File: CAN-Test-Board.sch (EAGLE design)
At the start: 52 parts, among them Y1 ECS-80-S-4X, Y2 ECS-80-S-4X

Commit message: couple part values
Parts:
- C12: value 100nF -> 0.1uF
- R14: value (none) -> 0
- R7, R9: value (none) -> 330
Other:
- moved on the sheet: R14
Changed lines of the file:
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@@
 <part name="R3" library="SparkFun-Resistors" library_urn="urn:adsk.eagle:library:532" deviceset="1KOHM" device="-0603-1/10W-1%" package3d_urn="urn:adsk.eagle:package:39650/1" value="1k"/>
 <part name="D1" library="SparkFun-LED" library_urn="urn:adsk.eagle:library:529" deviceset="LED" device="0603" package3d_urn="urn:adsk.eagle:package:39354/1"/>
-<part name="R7" library="SparkFun-Resistors" library_urn="urn:adsk.eagle:library:532" deviceset="RESISTOR" device="0603" package3d_urn="urn:adsk.eagle:package:39650/1" value=" "/>
+<part name="R7" library="SparkFun-Resistors" library_urn="urn:adsk.eagle:library:532" deviceset="RESISTOR" device="0603" package3d_urn="urn:adsk.eagle:package:39650/1" value="330"/>
 <part name="GND11" library="supply2" library_urn="urn:adsk.eagle:library:372" deviceset="GND" device=""/>
 <part name="FRAME2" library="SparkFun-Aesthetics" library_urn="urn:adsk.eagle:library:507" deviceset="FRAME-A4L" device=""/>
 <part name="U$1" library="PI_Shield_Library" deviceset="MCP2515" device=""/>
-<part name="C12" library="SparkFun-Capacitors" library_urn="urn:adsk.eagle:library:510" deviceset="22NF/22,000PF" device="-0603-50V-10%" package3d_urn="urn:adsk.eagle:package:37414@1/1" value="100nF"/>
+<part name="C12" library="SparkFun-Capacitors" library_urn="urn:adsk.eagle:library:510" deviceset="22NF/22,000PF" device="-0603-50V-10%" package3d_urn="urn:adsk.eagle:package:37414@1/1" value="0.1uF"/>
 <part name="GND5" library="supply1" library_urn="urn:adsk.eagle:library:371" deviceset="GND" device=""/>
 <part name="GND10" library="supply1" library_urn="urn:adsk.eagle:library:371" deviceset="GND" device=""/>
@@
 <part name="GND22" library="SparkFun-PowerSymbols" library_urn="urn:adsk.eagle:library:530" deviceset="GND" device=""/>
 <part name="D2" library="SparkFun-LED" library_urn="urn:adsk.eagle:library:529" deviceset="LED" device="0603" package3d_urn="urn:adsk.eagle:package:39354/1"/>
-<part name="R9" library="SparkFun-Resistors" library_urn="urn:adsk.eagle:library:532" deviceset="RESISTOR" device="0603" package3d_urn="urn:adsk.eagle:package:39650/1" value=" "/>
+<part name="R9" library="SparkFun-Resistors" library_urn="urn:adsk.eagle:library:532" deviceset="RESISTOR" device="0603" package3d_urn="urn:adsk.eagle:package:39650/1" value="330"/>
 <part name="GND23" library="supply2" library_urn="urn:adsk.eagle:library:372" deviceset="GND" device=""/>
 <part name="J1" library="SparkFun-Connectors" library_urn="urn:adsk.eagle:library:513" deviceset="CONN_12" device="" package3d_urn="urn:adsk.eagle:package:38169/1"/>
@@
 <part name="J4" library="SparkFun-Connectors" library_urn="urn:adsk.eagle:library:513" deviceset="CONN_03" device="" package3d_urn="urn:adsk.eagle:package:38063/1"/>
 <part name="J5" library="SparkFun-Connectors" library_urn="urn:adsk.eagle:library:513" deviceset="CONN_03" device="" package3d_urn="urn:adsk.eagle:package:38063/1"/>
-<part name="R14" library="SparkFun-Resistors" library_urn="urn:adsk.eagle:library:532" deviceset="RESISTOR" device="0603" package3d_urn="urn:adsk.eagle:package:39650/1" value=" "/>
+<part name="R14" library="SparkFun-Resistors" library_urn="urn:adsk.eagle:library:532" deviceset="RESISTOR" device="0603" package3d_urn="urn:adsk.eagle:package:39650/1" value="0"/>
 <part name="R15" library="SparkFun-Resistors" library_urn="urn:adsk.eagle:library:532" deviceset="RESISTOR" device="0603" package3d_urn="urn:adsk.eagle:package:39650/1" value="0"/>
 <part name="U$4" library="Samtec t2i" deviceset="T2I" device="" package3d_urn="urn:adsk.eagle:package:23194708/2"/>
@@
 <attribute name="NAME" x="20.32" y="137.668" size="1.778" layer="95" font="vector"/>
 </instance>
-<instance part="R14" gate="G$1" x="241.3" y="55.88" smashed="yes" rot="R180">
-<attribute name="NAME" x="241.3" y="54.356" size="1.778" layer="95" font="vector" rot="R180" align="bottom-center"/>
-<attribute name="VALUE" x="241.3" y="57.404" size="1.778" layer="96" font="vector" rot="R180" align="top-center"/>
+<instance part="R14" gate="G$1" x="241.3" y="55.88" smashed="yes" rot="MR0">
+<attribute name="NAME" x="241.3" y="57.404" size="1.778" layer="95" font="vector" rot="MR0" align="bottom-center"/>
+<attribute name="VALUE" x="241.3" y="54.356" size="1.778" layer="96" font="vector" rot="MR0" align="top-center"/>
 </instance>
 <instance part="U$4" gate="G$1" x="25.4" y="154.94" smashed="yes">

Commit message: couple changes for a possible rev 2 (led sizes, button footprint)
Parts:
- C13, C14: device Resistor_Capacitor:C0603C180J5GACTU -> SparkFun-Capacitors:22NF/22,000PF-0603-50V-10%
- C15: value 100nF -> 0.1uF
- D1, D2: value (none) -> LED-0805; device SparkFun-LED:LED0603 -> LED-0805:LED-0805
- RESET: value SWITCH -> DISCRETECOMPONENTS_SWITCH; device DiscreteComponents:SWITCH -> Push button:DISCRETECOMPONENTS_SWITCH

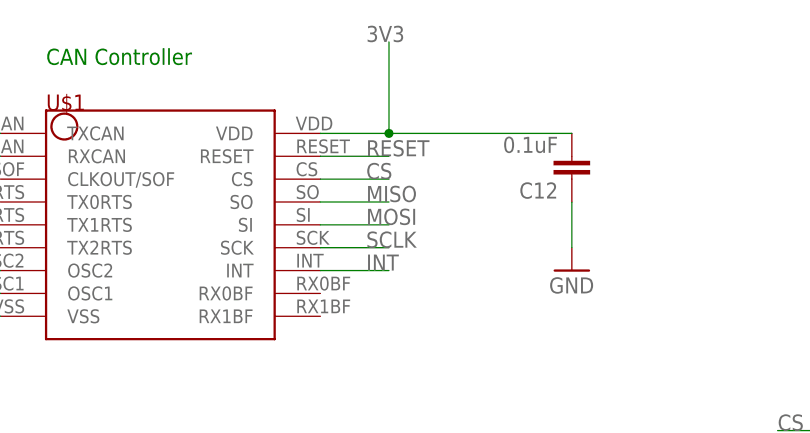
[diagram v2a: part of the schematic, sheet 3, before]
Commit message: Shorted Reset to 3V3 instead of leaving it floating
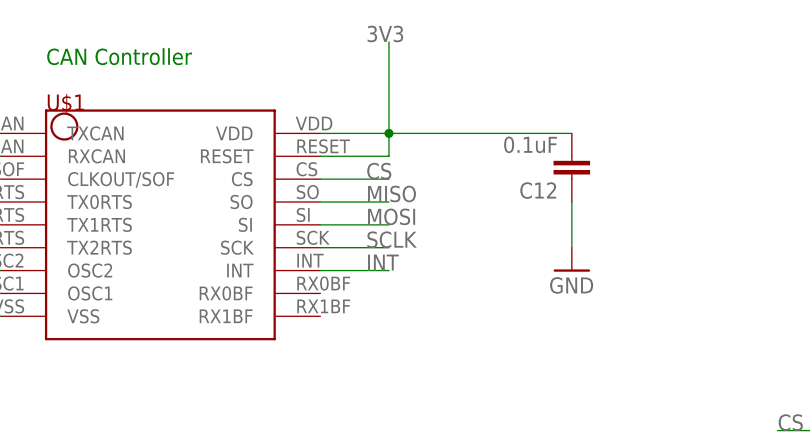
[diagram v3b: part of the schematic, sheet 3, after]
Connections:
- removed net RESET: U$1.RESET
- net 3V3: now also U$1.RESET
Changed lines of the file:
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@@
-</segment>
-</net>
-<net name="RESET" class="0">
-<segment>
-<pinref part="U$1" gate="G$1" pin="RESET"/>
-<wire x1="193.04" y1="162.56" x2="200.66" y2="162.56" width="0.1524" layer="91"/>
-<label x="198.12" y="162.56" size="1.778" layer="95"/>
 </segment>
 </net>
@@
 <junction x="200.66" y="165.1"/>
 <label x="198.12" y="175.26" size="1.778" layer="95"/>
+<pinref part="U$1" gate="G$1" pin="RESET"/>
+<wire x1="193.04" y1="162.56" x2="200.66" y2="162.56" width="0.1524" layer="91"/>
+<wire x1="200.66" y1="162.56" x2="200.66" y2="165.1" width="0.1524" layer="91"/>
 </segment>
 <segment>

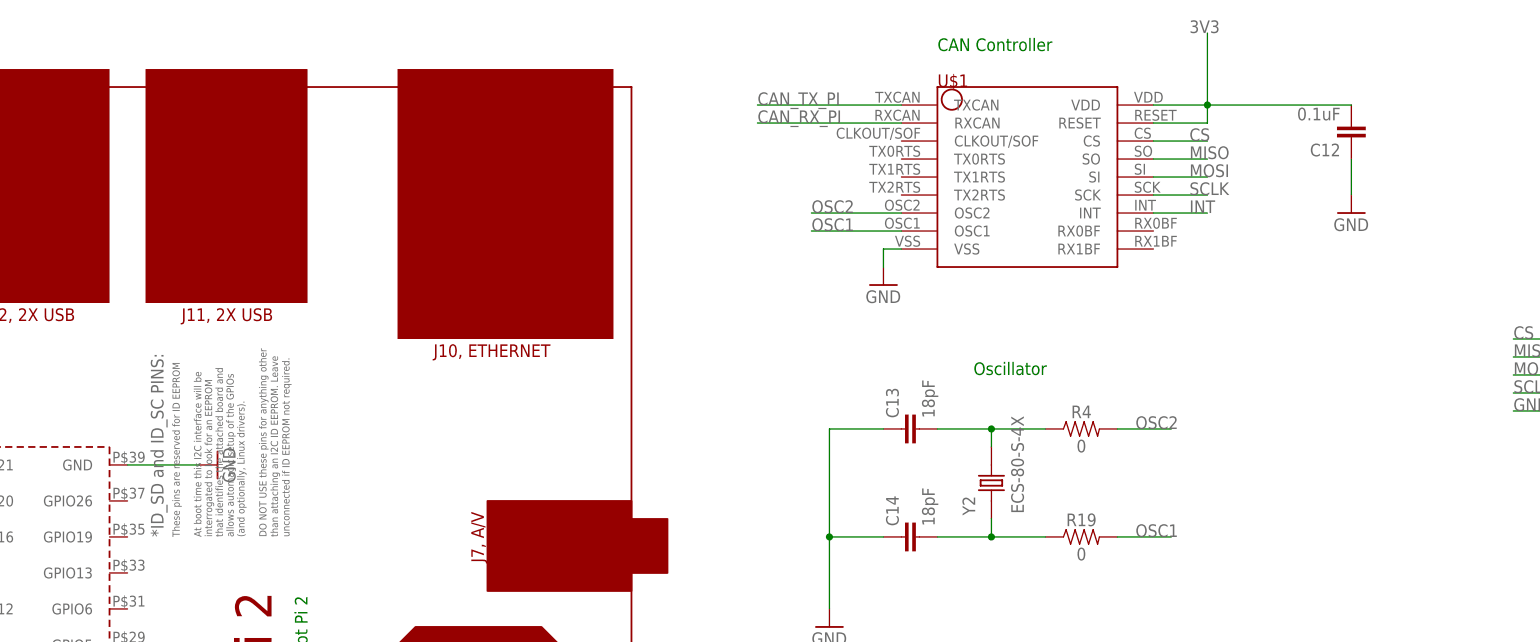
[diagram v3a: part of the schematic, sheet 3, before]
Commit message: Add missing interrupt connection
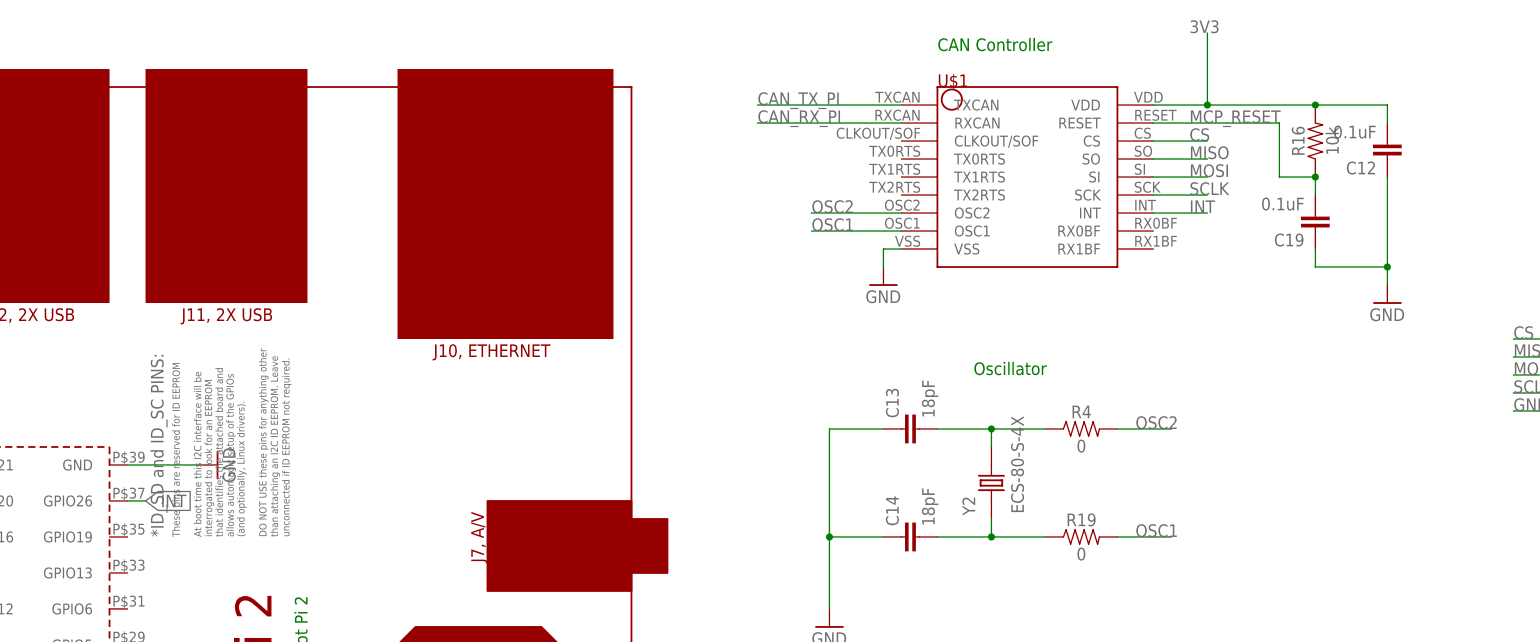
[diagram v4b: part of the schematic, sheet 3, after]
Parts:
- added C19: 0.1uF, SparkFun-Capacitors:22NF/22,000PF-0603-50V-10%
- added R16: 10k, SparkFun-Resistors:1KOHM-0603-1/10W-1%
- C7: value 4.7uF -> 0.1uF
- R2: value 1k -> 10k
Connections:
- new net MCP_RESET: C19.2, R16.1, U$1.RESET
- net 3V3: now also R16.2; no longer U$1.RESET
- net GND: now also C19.1
- net INT: now also PCB1.GPIO26
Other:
- moved on the sheet: C12
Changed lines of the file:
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@@
 <?xml version="1.0" encoding="utf-8"?>
 <!DOCTYPE eagle SYSTEM "eagle.dtd">
-<eagle version="9.6.2">
+<eagle version="9.6.0">
 <drawing>
 <settings>
@@
 <part name="GND1" library="supply2" library_urn="urn:adsk.eagle:library:372" deviceset="GND" device=""/>
 <part name="GND2" library="supply2" library_urn="urn:adsk.eagle:library:372" deviceset="GND" device=""/>
-<part name="C7" library="SparkFun-Capacitors" library_urn="urn:adsk.eagle:library:510" deviceset="4.7UF" device="0603" package3d_urn="urn:adsk.eagle:package:37414@2/1" value="4.7uF"/>
+<part name="C7" library="SparkFun-Capacitors" library_urn="urn:adsk.eagle:library:510" deviceset="4.7UF" device="0603" package3d_urn="urn:adsk.eagle:package:37414@2/1" value="0.1uF"/>
 <part name="GND3" library="supply2" library_urn="urn:adsk.eagle:library:372" deviceset="GND" device=""/>
 <part name="SV1" library="con-lsta" library_urn="urn:adsk.eagle:library:161" deviceset="FE05-1" device="" package3d_urn="urn:adsk.eagle:package:8190/1"/>
@@
 <part name="R1" library="SparkFun-Resistors" library_urn="urn:adsk.eagle:library:532" deviceset="1KOHM" device="-0603-1/10W-1%" package3d_urn="urn:adsk.eagle:package:39650/1" value="1k"/>
 <part name="+3V1" library="supply1" library_urn="urn:adsk.eagle:library:371" deviceset="+3V3" device=""/>
-<part name="R2" library="SparkFun-Resistors" library_urn="urn:adsk.eagle:library:532" deviceset="1KOHM" device="-0603-1/10W-1%" package3d_urn="urn:adsk.eagle:package:39650/1" value="1k"/>
+<part name="R2" library="SparkFun-Resistors" library_urn="urn:adsk.eagle:library:532" deviceset="1KOHM" device="-0603-1/10W-1%" package3d_urn="urn:adsk.eagle:package:39650/1" value="10k"/>
 <part name="+3V2" library="supply1" library_urn="urn:adsk.eagle:library:371" deviceset="+3V3" device=""/>
 <part name="R3" library="SparkFun-Resistors" library_urn="urn:adsk.eagle:library:532" deviceset="1KOHM" device="-0603-1/10W-1%" package3d_urn="urn:adsk.eagle:package:39650/1" value="1k"/>
@@
 <part name="D2" library="LED-0805" deviceset="LED-0805" device=""/>
 <part name="RESET" library="Push button" deviceset="DISCRETECOMPONENTS_SWITCH" device=""/>
+<part name="C19" library="SparkFun-Capacitors" library_urn="urn:adsk.eagle:library:510" deviceset="22NF/22,000PF" device="-0603-50V-10%" package3d_urn="urn:adsk.eagle:package:37414@1/1" value="0.1uF"/>
+<part name="R16" library="SparkFun-Resistors" library_urn="urn:adsk.eagle:library:532" deviceset="1KOHM" device="-0603-1/10W-1%" package3d_urn="urn:adsk.eagle:package:39650/1" value="10k"/>
 </parts>
 <sheets>
@@
 <attribute name="NAME" x="162.56" y="167.64" size="1.778" layer="94"/>
 </instance>
-<instance part="C12" gate="G$1" x="220.98" y="162.56" smashed="yes" rot="R180">
-<attribute name="NAME" x="219.456" y="159.639" size="1.778" layer="95" font="vector" rot="R180"/>
-<attribute name="VALUE" x="219.456" y="164.719" size="1.778" layer="96" font="vector" rot="R180"/>
-</instance>
-<instance part="GND5" gate="1" x="220.98" y="149.86" smashed="yes">
-<attribute name="VALUE" x="218.44" y="147.32" size="1.778" layer="96"/>
+<instance part="C12" gate="G$1" x="226.06" y="160.02" smashed="yes" rot="R180">
+<attribute name="NAME" x="224.536" y="157.099" size="1.778" layer="95" font="vector" rot="R180"/>
+<attribute name="VALUE" x="224.536" y="162.179" size="1.778" layer="96" font="vector" rot="R180"/>
+</instance>
+<instance part="GND5" gate="1" x="226.06" y="137.16" smashed="yes">
+<attribute name="VALUE" x="223.52" y="134.62" size="1.778" layer="96"/>
 </instance>
 <instance part="GND10" gate="1" x="154.94" y="139.7" smashed="yes">
@@
 <attribute name="NAME" x="157.099" y="105.664" size="1.778" layer="95" font="vector" rot="R90"/>
 <attribute name="VALUE" x="162.179" y="105.664" size="1.778" layer="96" font="vector" rot="R90"/>
+</instance>
+<instance part="C19" gate="G$1" x="215.9" y="149.86" smashed="yes" rot="R180">
+<attribute name="NAME" x="214.376" y="146.939" size="1.778" layer="95" font="vector" rot="R180"/>
+<attribute name="VALUE" x="214.376" y="152.019" size="1.778" layer="96" font="vector" rot="R180"/>
+</instance>
+<instance part="R16" gate="G$1" x="215.9" y="160.02" smashed="yes" rot="R90">
+<attribute name="NAME" x="214.376" y="160.02" size="1.778" layer="95" font="vector" rot="R90" align="bottom-center"/>
+<attribute name="VALUE" x="217.424" y="160.02" size="1.778" layer="96" font="vector" rot="R90" align="top-center"/>
 </instance>
 </instances>
@@
 <segment>
 <pinref part="C12" gate="G$1" pin="1"/>
-<wire x1="220.98" y1="157.48" x2="220.98" y2="152.4" width="0.1524" layer="91"/>
+<wire x1="226.06" y1="154.94" x2="226.06" y2="142.24" width="0.1524" layer="91"/>
 <pinref part="GND5" gate="1" pin="GND"/>
+<pinref part="C19" gate="G$1" pin="1"/>
+<wire x1="226.06" y1="142.24" x2="226.06" y2="139.7" width="0.1524" layer="91"/>
+<wire x1="215.9" y1="144.78" x2="215.9" y2="142.24" width="0.1524" layer="91"/>
+<wire x1="215.9" y1="142.24" x2="226.06" y2="142.24" width="0.1524" layer="91"/>
+<junction x="226.06" y="142.24"/>
 </segment>
 <segment>
@@
 <label x="198.12" y="149.86" size="1.778" layer="95"/>
 </segment>
+<segment>
+<pinref part="PCB1" gate="G$1" pin="GPIO26"/>
+<wire x1="48.26" y1="109.22" x2="50.8" y2="109.22" width="0.1524" layer="91"/>
+<label x="50.8" y="109.22" size="1.778" layer="95" xref="yes"/>
+</segment>
 </net>
 <net name="3V3" class="2">
@@
 <wire x1="200.66" y1="165.1" x2="200.66" y2="175.26" width="0.1524" layer="91"/>
 <pinref part="C12" gate="G$1" pin="2"/>
-<wire x1="200.66" y1="165.1" x2="220.98" y2="165.1" width="0.1524" layer="91"/>
+<wire x1="200.66" y1="165.1" x2="215.9" y2="165.1" width="0.1524" layer="91"/>
+<wire x1="215.9" y1="165.1" x2="226.06" y2="165.1" width="0.1524" layer="91"/>
+<wire x1="226.06" y1="165.1" x2="226.06" y2="162.56" width="0.1524" layer="91"/>
 <junction x="200.66" y="165.1"/>
 <label x="198.12" y="175.26" size="1.778" layer="95"/>
-<pinref part="U$1" gate="G$1" pin="RESET"/>
-<wire x1="193.04" y1="162.56" x2="200.66" y2="162.56" width="0.1524" layer="91"/>
-<wire x1="200.66" y1="162.56" x2="200.66" y2="165.1" width="0.1524" layer="91"/>
+<pinref part="R16" gate="G$1" pin="2"/>
+<junction x="215.9" y="165.1"/>
 </segment>
 <segment>
@@
 </segment>
 </net>
+<net name="MCP_RESET" class="0">
+<segment>
+<pinref part="U$1" gate="G$1" pin="RESET"/>
+<wire x1="193.04" y1="162.56" x2="210.82" y2="162.56" width="0.1524" layer="91"/>
+<wire x1="210.82" y1="162.56" x2="210.82" y2="154.94" width="0.1524" layer="91"/>
+<pinref part="R16" gate="G$1" pin="1"/>
+<wire x1="210.82" y1="154.94" x2="215.9" y2="154.94" width="0.1524" layer="91"/>
+<pinref part="C19" gate="G$1" pin="2"/>
+<wire x1="215.9" y1="154.94" x2="215.9" y2="152.4" width="0.1524" layer="91"/>
+<junction x="215.9" y="154.94"/>
+<label x="198.12" y="162.56" size="1.778" layer="95"/>
+</segment>
+</net>
